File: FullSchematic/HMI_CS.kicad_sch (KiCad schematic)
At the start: 18 parts, among them Q4 BSS138-7-F, U7 Current Sensor, U8 Op Amp

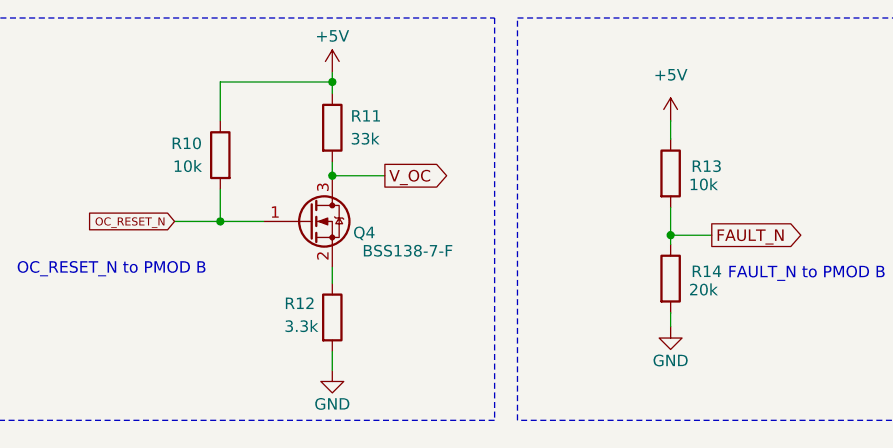
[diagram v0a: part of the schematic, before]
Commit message: Schematic/Footprint Update
Corrected Footprint / Schematic for PCB Design and Changed 10k Resistors to 0603 size.
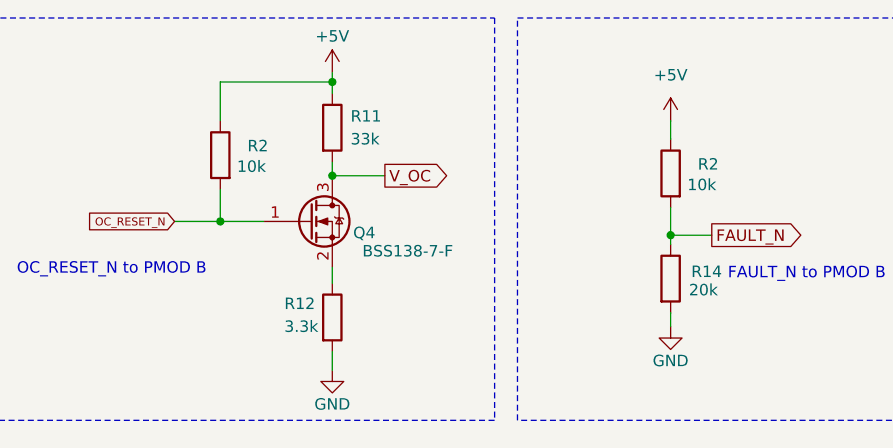
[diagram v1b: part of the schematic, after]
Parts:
- removed R10, R13: 10k, Resistor_SMD:R_1206_3216Metric, symbol Device:R
- added R2 (x2): 10k, Resistor_SMD:R_0201_0603Metric, symbol Device:R
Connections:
- net +5V: now also R2.1, R2.1
- net FAULT_N: now also R2.2
- net OC_RESET_N: now also R2.2
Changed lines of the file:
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@@
-    )
-  )
-  (symbol (lib_id "Device:R") (at 93.218 37.846 0) (mirror y) (unit 1)
-    (in_bom yes) (on_board yes) (dnp no)
-    (property "Reference" "R10" (at 91.186 36.576 0)
-      (effects (font (size 1.27 1.27)) (justify left))
-    )
-    (property "Value" "10k" (at 91.186 39.116 0)
-      (effects (font (size 1.27 1.27)) (justify left))
-    )
-    (property "Footprint" "Resistor_SMD:R_1206_3216Metric" (at 94.996 37.846 90)
-      (effects (font (size 1.27 1.27)) hide)
-    )
-    (property "Datasheet" "~" (at 93.218 37.846 0)
-      (effects (font (size 1.27 1.27)) hide)
-    )
-    (property "SEL P/N" "255-1002" (at 93.218 37.846 0)
-      (effects (font (size 1.27 1.27)) hide)
-    )
-    (property "MFG P/N" "CRCW120610K0FKEA" (at 93.218 37.846 0)
-      (effects (font (size 1.27 1.27)) hide)
-    )
-    (pin "1")
-    (pin "2")
-    (instances
-      (project "FullSchematic"
-        (path "/650f0e66-3493-4c97-9577-99f99fcd23df/3542ca37-4624-4740-af78-19651a951512"
-          (reference "R10") (unit 1)
-        )
-      )
-      (project "Senior Design HMI Schematic R2 20230722_MB"
-        (path "/8c847d65-180e-4b65-a3db-30ced04c6f38"
-          (reference "R25") (unit 1)
-        )
-        (path "/8c847d65-180e-4b65-a3db-30ced04c6f38/74cc473d-d4c1-4a03-a7be-fcad9d3b3420"
-          (reference "R9") (unit 1)
-        )
-      )
     )
   )
@@
     )
   )
+  (symbol (lib_id "Device:R") (at 143.256 39.878 0) (mirror y) (unit 1)
+    (in_bom yes) (on_board yes) (dnp no)
+    (property "Reference" "R2" (at 148.59 38.862 0)
+      (effects (font (size 1.27 1.27)) (justify left))
+    )
+    (property "Value" "10k" (at 148.336 41.148 0)
+      (effects (font (size 1.27 1.27)) (justify left))
+    )
+    (property "Footprint" "Resistor_SMD:R_0201_0603Metric" (at 145.034 39.878 90)
+      (effects (font (size 1.27 1.27)) hide)
+    )
+    (property "Datasheet" "~" (at 143.256 39.878 0)
+      (effects (font (size 1.27 1.27)) hide)
+    )
+    (property "SEL P/N" "252-1002" (at 143.256 39.878 0)
+      (effects (font (size 1.27 1.27)) hide)
+    )
+    (property "MFG P/N" "CRCW060310K0FKEB" (at 143.256 39.878 0)
+      (effects (font (size 1.27 1.27)) hide)
+    )
+    (pin "1")
+    (pin "2")
+    (instances
+      (project "FullSchematic"
+        (path "/650f0e66-3493-4c97-9577-99f99fcd23df"
+          (reference "R2") (unit 1)
+        )
+        (path "/650f0e66-3493-4c97-9577-99f99fcd23df/3542ca37-4624-4740-af78-19651a951512"
+          (reference "R13") (unit 1)
+        )
+      )
+      (project "Senior Design HMI Schematic R2 20230722_MB"
+        (path "/8c847d65-180e-4b65-a3db-30ced04c6f38"
+          (reference "R30") (unit 1)
+        )
+        (path "/8c847d65-180e-4b65-a3db-30ced04c6f38/2dcf8d52-10d8-44ca-a916-d85406e99c43"
+          (reference "R6") (unit 1)
+        )
+      )
+    )
+  )
   (symbol (lib_id "Device:C") (at 180.086 111.506 0) (unit 1)
     (in_bom yes) (on_board yes) (dnp no)
@@
     )
   )
-  (symbol (lib_id "Device:R") (at 143.256 39.878 0) (unit 1)
-    (in_bom yes) (on_board yes) (dnp no)
-    (property "Reference" "R13" (at 145.542 39.116 0)
-      (effects (font (size 1.27 1.27)) (justify left))
-    )
-    (property "Value" "10k" (at 145.288 41.148 0)
-      (effects (font (size 1.27 1.27)) (justify left))
-    )
-    (property "Footprint" "Resistor_SMD:R_1206_3216Metric" (at 141.478 39.878 90)
-      (effects (font (size 1.27 1.27)) hide)
-    )
-    (property "Datasheet" "~" (at 143.256 39.878 0)
-      (effects (font (size 1.27 1.27)) hide)
-    )
-    (property "SEL P/N" "255-1002" (at 143.256 39.878 0)
-      (effects (font (size 1.27 1.27)) hide)
-    )
-    (property "MFG P/N" "CRCW120610K0FKEA" (at 143.256 39.878 0)
-      (effects (font (size 1.27 1.27)) hide)
-    )
-    (pin "1")
-    (pin "2")
-    (instances
-      (project "FullSchematic"
-        (path "/650f0e66-3493-4c97-9577-99f99fcd23df/3542ca37-4624-4740-af78-19651a951512"
-          (reference "R13") (unit 1)
-        )
-      )
-      (project "Senior Design HMI Schematic R2 20230722_MB"
-        (path "/8c847d65-180e-4b65-a3db-30ced04c6f38"
-          (reference "R18") (unit 1)
-        )
-        (path "/8c847d65-180e-4b65-a3db-30ced04c6f38/74cc473d-d4c1-4a03-a7be-fcad9d3b3420"
-          (reference "R12") (unit 1)
-        )
-      )
-    )
-  )
   (symbol (lib_id "power:+5V") (at 143.256 34.036 0) (unit 1)
     (in_bom yes) (on_board yes) (dnp no) (fields_autoplaced)
@@
         )
       )
+    )
+  )
+  (symbol (lib_id "Device:R") (at 93.218 37.846 0) (mirror y) (unit 1)
+    (in_bom yes) (on_board yes) (dnp no)
+    (property "Reference" "R2" (at 98.552 36.83 0)
+      (effects (font (size 1.27 1.27)) (justify left))
+    )
+    (property "Value" "10k" (at 98.298 39.116 0)
+      (effects (font (size 1.27 1.27)) (justify left))
+    )
+    (property "Footprint" "Resistor_SMD:R_0201_0603Metric" (at 94.996 37.846 90)
+      (effects (font (size 1.27 1.27)) hide)
+    )
+    (property "Datasheet" "~" (at 93.218 37.846 0)
+      (effects (font (size 1.27 1.27)) hide)
+    )
+    (property "SEL P/N" "252-1002" (at 93.218 37.846 0)
+      (effects (font (size 1.27 1.27)) hide)
+    )
+    (property "MFG P/N" "CRCW060310K0FKEB" (at 93.218 37.846 0)
+      (effects (font (size 1.27 1.27)) hide)
+    )
+    (pin "1")
+    (pin "2")
+    (instances
+      (project "FullSchematic"
+        (path "/650f0e66-3493-4c97-9577-99f99fcd23df"
+          (reference "R2") (unit 1)
+        )
+        (path "/650f0e66-3493-4c97-9577-99f99fcd23df/3542ca37-4624-4740-af78-19651a951512"
+          (reference "R10") (unit 1)
+        )
+      )
+      (project "Senior Design HMI Schematic R2 20230722_MB"
+        (path "/8c847d65-180e-4b65-a3db-30ced04c6f38"
+          (reference "R30") (unit 1)
+        )
+        (path "/8c847d65-180e-4b65-a3db-30ced04c6f38/2dcf8d52-10d8-44ca-a916-d85406e99c43"
+          (reference "R6") (unit 1)
+        )
+      )

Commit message: More Edits
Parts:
- R11: footprint Resistor_SMD:R_0402_1005Metric -> Resistor_SMD:R_0603_1608Metric; MFG P/N CRCW040233K0FKED -> RMCF0603JT33K0; SEL P/N 463-33K0 -> 462-33K0
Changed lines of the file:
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@@
       (effects (font (size 1.27 1.27)) (justify left))
     )
-    (property "Footprint" "Resistor_SMD:R_0402_1005Metric" (at 103.886 34.798 90)
+    (property "Footprint" "Resistor_SMD:R_0603_1608Metric" (at 103.886 34.798 90)
       (effects (font (size 1.27 1.27)) hide)
     )
@@
       (effects (font (size 1.27 1.27)) hide)
     )
-    (property "SEL P/N" "463-33K0" (at 105.664 34.798 0)
+    (property "SEL P/N" "462-33K0 " (at 105.664 34.798 0)
       (effects (font (size 1.27 1.27)) hide)
     )
-    (property "MFG P/N" "CRCW040233K0FKED" (at 105.664 34.798 0)
+    (property "MFG P/N" "RMCF0603JT33K0" (at 105.664 34.798 0)
       (effects (font (size 1.27 1.27)) hide)
     )
@@
           (reference "R11") (unit 1)
         )
+        (path "/650f0e66-3493-4c97-9577-99f99fcd23df"
+          (reference "R11") (unit 1)
+        )
